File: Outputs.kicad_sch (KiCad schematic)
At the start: 44 parts, among them J5 OUT1, J6 OUT2, J7 OUT3, J8 OUT4

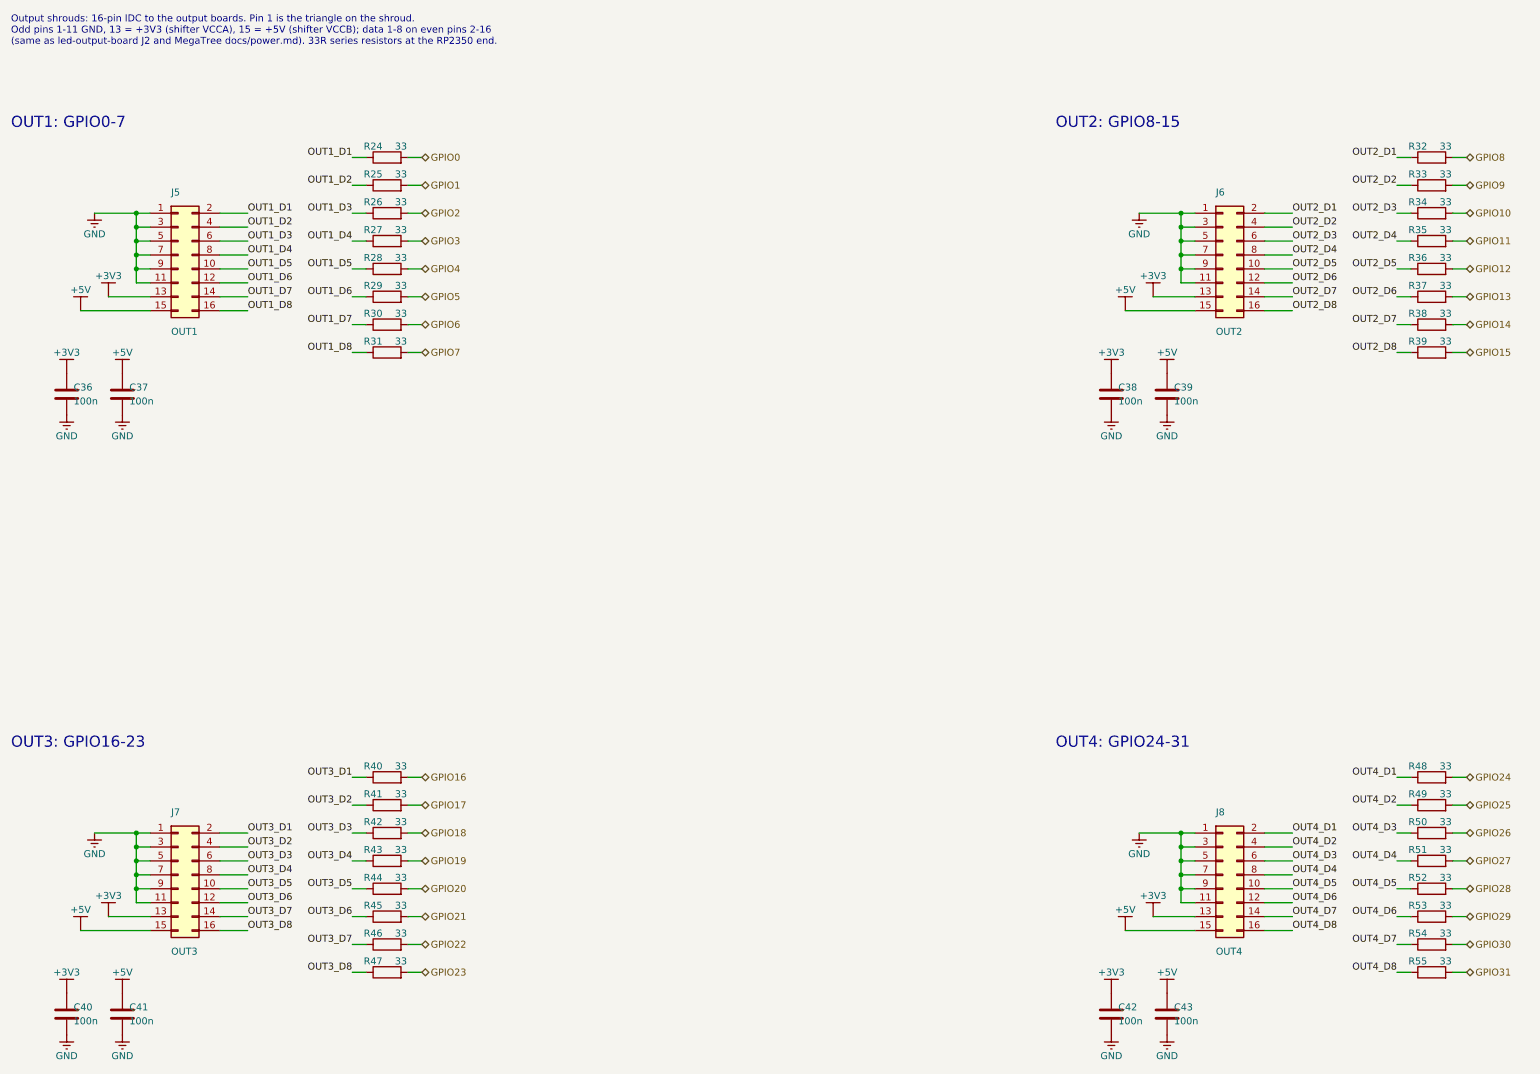
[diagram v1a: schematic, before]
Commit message: Wire the 33R resistors straight to the shroud pins
Drops the OUTk_Dn net labels between each shroud pin and its resistor.

Co-Authored-By: Claude Opus 5.5 (1M context) <noreply@anthropic.com>
Claude-Session: https://claude.ai/code/session_01CYnkeL97vxsPSCyXSKGro9
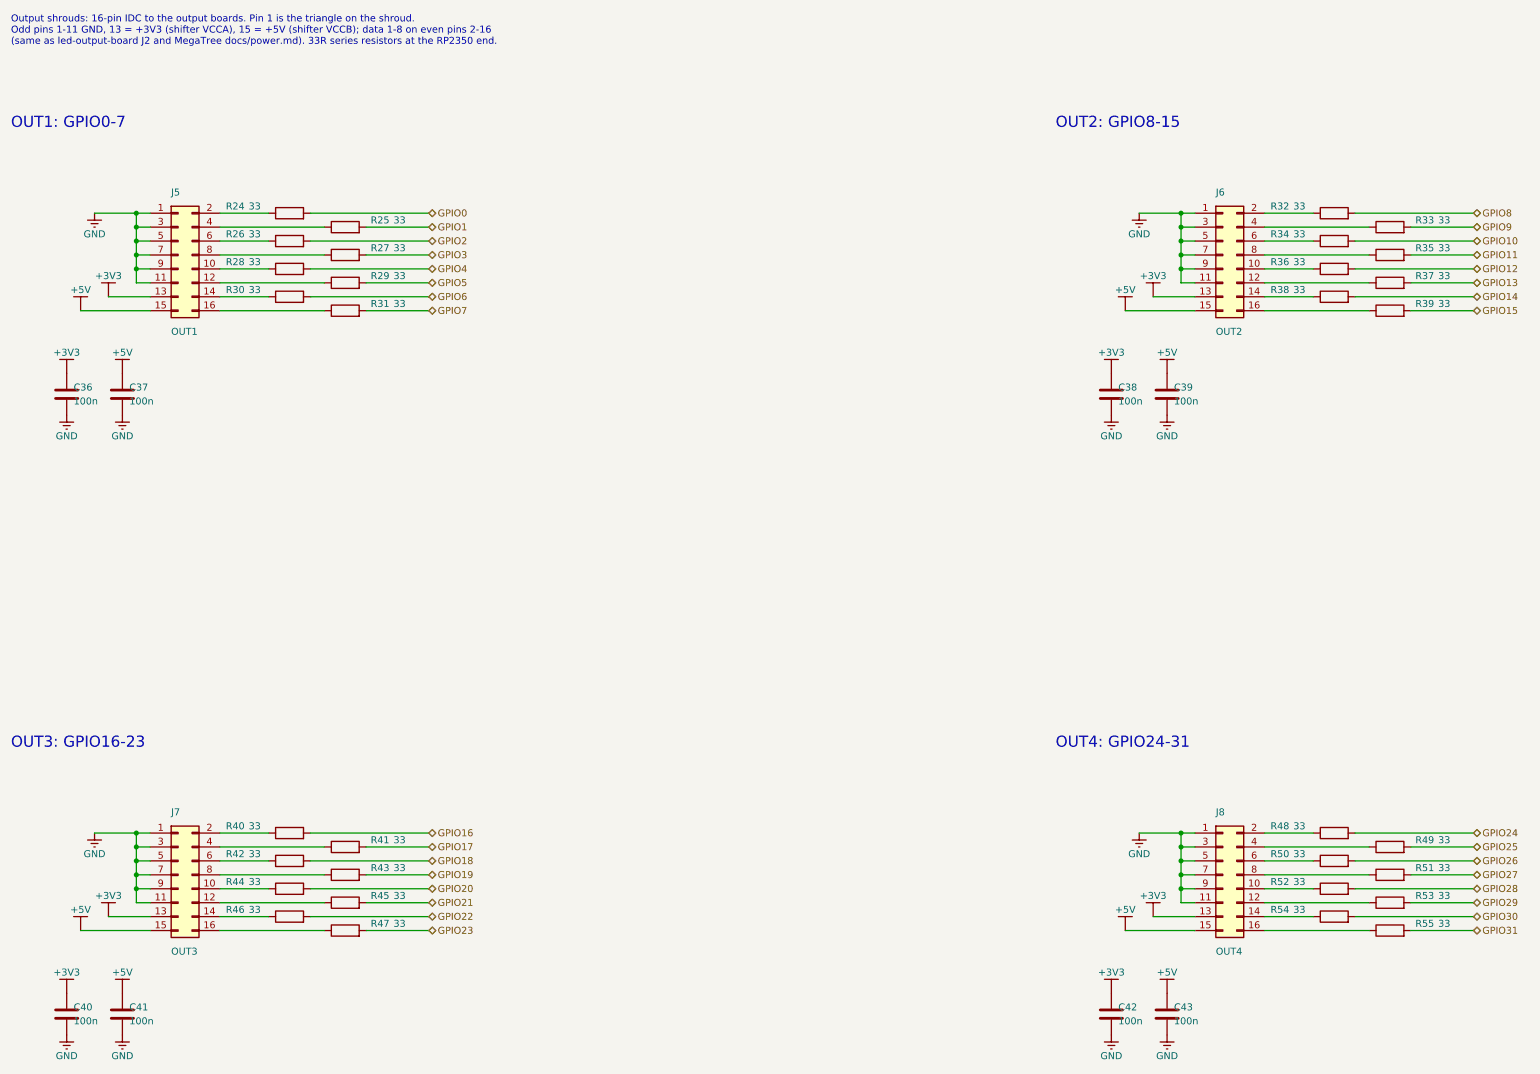
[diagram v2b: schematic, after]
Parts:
- removed R50: 33, Resistor_SMD:R_0402_1005Metric, symbol Device:R
- added R47: 33, Resistor_SMD:R_0402_1005Metric, symbol Device:R
- renumbered R47 to R50
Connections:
- net GPIO23: now also R47.2; no longer R50.2
- net GPIO26: now also R50.2
- net OUT1_D1: no longer names the net of J5.2 (Pin_2), R24.1
- net OUT1_D2: no longer names the net of J5.4 (Pin_4), R25.1
- net OUT1_D3: no longer names the net of J5.6 (Pin_6), R26.1
- net OUT1_D4: no longer names the net of J5.8 (Pin_8), R27.1
- net OUT1_D5: no longer names the net of J5.10 (Pin_10), R28.1
- net OUT1_D6: no longer names the net of J5.12 (Pin_12), R29.1
- net OUT1_D7: no longer names the net of J5.14 (Pin_14), R30.1
- net OUT1_D8: no longer names the net of J5.16 (Pin_16), R31.1
- net OUT2_D1: no longer names the net of J6.2 (Pin_2), R32.1
- net OUT2_D2: no longer names the net of J6.4 (Pin_4), R33.1
- net OUT2_D3: no longer names the net of J6.6 (Pin_6), R34.1
- net OUT2_D4: no longer names the net of J6.8 (Pin_8), R35.1
- net OUT2_D5: no longer names the net of J6.10 (Pin_10), R36.1
- net OUT2_D6: no longer names the net of J6.12 (Pin_12), R37.1
- net OUT2_D7: no longer names the net of J6.14 (Pin_14), R38.1
- net OUT2_D8: no longer names the net of J6.16 (Pin_16), R39.1
- net OUT3_D1: no longer names the net of J7.2 (Pin_2), R40.1
- net OUT3_D2: no longer names the net of J7.4 (Pin_4), R41.1
- net OUT3_D3: no longer names the net of J7.6 (Pin_6), R42.1
- net OUT3_D4: no longer names the net of J7.8 (Pin_8), R43.1
- net OUT3_D5: no longer names the net of J7.10 (Pin_10), R44.1
- net OUT3_D6: no longer names the net of J7.12 (Pin_12), R45.1
- net OUT3_D7: no longer names the net of J7.14 (Pin_14), R46.1
- net OUT3_D8: no longer names the net of J7.16 (Pin_16)
- net OUT3_D8: now also R47.1; no longer R50.1
- net OUT4_D1: no longer names the net of J8.2 (Pin_2), R48.1
- net OUT4_D2: no longer names the net of J8.4 (Pin_4), R49.1
- net OUT4_D3: no longer names the net of J8.6 (Pin_6)
- net OUT4_D3: now also R50.1
- net OUT4_D4: no longer names the net of J8.8 (Pin_8), R51.1
- net OUT4_D5: no longer names the net of J8.10 (Pin_10), R52.1
- net OUT4_D6: no longer names the net of J8.12 (Pin_12), R53.1
- net OUT4_D7: no longer names the net of J8.14 (Pin_14), R54.1
- net OUT4_D8: no longer names the net of J8.16 (Pin_16), R55.1
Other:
- moved on the sheet: R50
